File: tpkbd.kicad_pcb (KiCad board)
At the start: 2 copper layers, 43 x 38 mm, 21 parts, among them CON1 AVR-ISP-6, J1 CONN_01X02, J2 CONN_01X01, J3 USB_OTG, J4 CONN_02X20, J5 CONN_01X04, J6 GS2, J7 0, U1 ATMEGA8515-16AU, U2 AP111733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

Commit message: cleanup
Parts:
- removed CON1: AVR-ISP-6, Pin_Headers:Pin_Header_Straight_2x03
- added D1: LED, KX14:PLCC4, F.Cu at (64.6, 29.2)
- added J8: CONN_01X06, Pin_Headers:Pin_Header_Straight_1x06, F.Cu at (55.9, 59.7)
- added R6: R, Resistors_SMD:R_0603_HandSoldering, F.Cu at (63.6, 32.3)
- added R7: R, Resistors_SMD:R_0603_HandSoldering, F.Cu at (62.2, 53.2)
- added R8: R, Resistors_SMD:R_0603_HandSoldering, F.Cu at (66.8, 31.6)
- C1, C2: footprint Capacitors_SMD:C_0805_HandSoldering -> Capacitors_SMD:C_0603_HandSoldering
- C3: footprint Capacitors_SMD:C_0402 -> Capacitors_SMD:C_0603_HandSoldering
- J2: footprint Pin_Headers:Pin_Header_Straight_1x01 -> KX14:Pins1x1
- J4: value CONN_02X20 -> CONN_02X21
- R1, R2, R3, R4, R5: footprint Resistors_SMD:R_0805_HandSoldering -> Resistors_SMD:R_0603_HandSoldering
- moved J5 23.8 mm to (64.0, 26.6), turned to 90 degrees
- moved C4 10.8 mm to (55.2, 42.0), turned to 270 degrees
- moved R3 7.15 mm to (58.1, 42.1)
- moved R2 7.05 mm to (60.6, 42.1)
- moved U2 6.00 mm to (58.4, 36.0), turned to 270 degrees
- moved R4 4.77 mm to (60.6, 31.4), turned to 180 degrees
- moved C5 4.75 mm to (64.1, 39.7), turned to 45 degrees
- moved J3 4.04 mm to (57.6, 27.6)
- moved R1 3.62 mm to (63.6, 44.5), turned to 315 degrees
- moved J7 2.39 mm to (54.9, 31.4), turned to 270 degrees
- moved J2 1.17 mm to (56.4, 31.6)
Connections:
- J4 pad 42: (no net) -> Net-(J4-Pad42)
- J5 pad 1: +3V3 -> +5V
- U1 pad 10: /kb_id0 -> Net-(R3-Pad2)
- U1 pad 9: Net-(R3-Pad2) -> /led
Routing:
- net /led: track 0.00 -> 39.8 mm
- net +5V: track 79.9 -> 113.5 mm
- net /tp_rst_b: track 56.6 -> 88.4 mm, vias 2 -> 3
- net Net-(R3-Pad2): track 51.2 -> 20.2 mm
- net Net-(R2-Pad2): track 42.6 -> 15.0 mm
- net Net-(J5-Pad2): track 10.0 -> 34.9 mm
- net Net-(J3-Pad3): track 6.49 -> 19.7 mm
- net /power: track 50.2 -> 57.5 mm
- net +3V3: track 110.1 -> 103.0 mm, vias 3 -> 4
- net Net-(J3-Pad2): track 8.11 -> 13.7 mm
- net /kb_id0: track 41.7 -> 47.2 mm
- net GND: track 162.3 -> 167.2 mm, vias 1 -> 0
- net Net-(J2-Pad1): track 6.95 -> 2.37 mm
- net /B5: track 30.6 -> 34.1 mm
- net /kb_id1: track 41.6 -> 44.9 mm
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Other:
- net class Default: clearance 0.235 -> 0.3
- rule trace_clearance: 0.235 -> 0.3

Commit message: cleanup2
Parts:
- removed J1: CONN_01X02, Buttons_Switches_SMD:SW_SPST_FSMSM
- J8: value CONN_01X06 -> CONN_01X05; footprint Pin_Headers:Pin_Header_Straight_1x06 -> KX14:Pins_1x5
- moved J8 10.2 mm to (62.0, 51.5), turned to 150 degrees
- moved R7 2.59 mm to (60.8, 55.4)
- moved R1 1.30 mm to (62.4, 45.0), turned to 270 degrees
- moved C5 0.51 mm to (64.2, 39.2)
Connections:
- J4 pad 42: Net-(J4-Pad42) -> GND
- U1 pad 6: (no net) -> GND
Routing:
- net GND: track 167.2 -> 189.6 mm
- net /B5: track 34.1 -> 13.6 mm, vias 1 -> 0
- net /B7: track 32.5 -> 17.2 mm, vias 1 -> 0
- net /RST: track 23.4 -> 10.0 mm, vias 1 -> 0
- net /B6: track 28.0 -> 16.0 mm, vias 1 -> 0
- net +5V: track 113.5 -> 104.1 mm
- net /tp_rst_b: track 88.4 -> 95.5 mm
- net Net-(R2-Pad2): track 15.0 -> 19.8 mm
- net /led: track 39.8 -> 44.4 mm
- net Net-(R3-Pad2): track 20.2 -> 24.7 mm
- net Net-(J5-Pad2): track 34.9 -> 38.3 mm
- net +3V3: track 103.0 -> 100.3 mm, vias 4 -> 3
- net /kb_id0: track 47.2 -> 48.7 mm

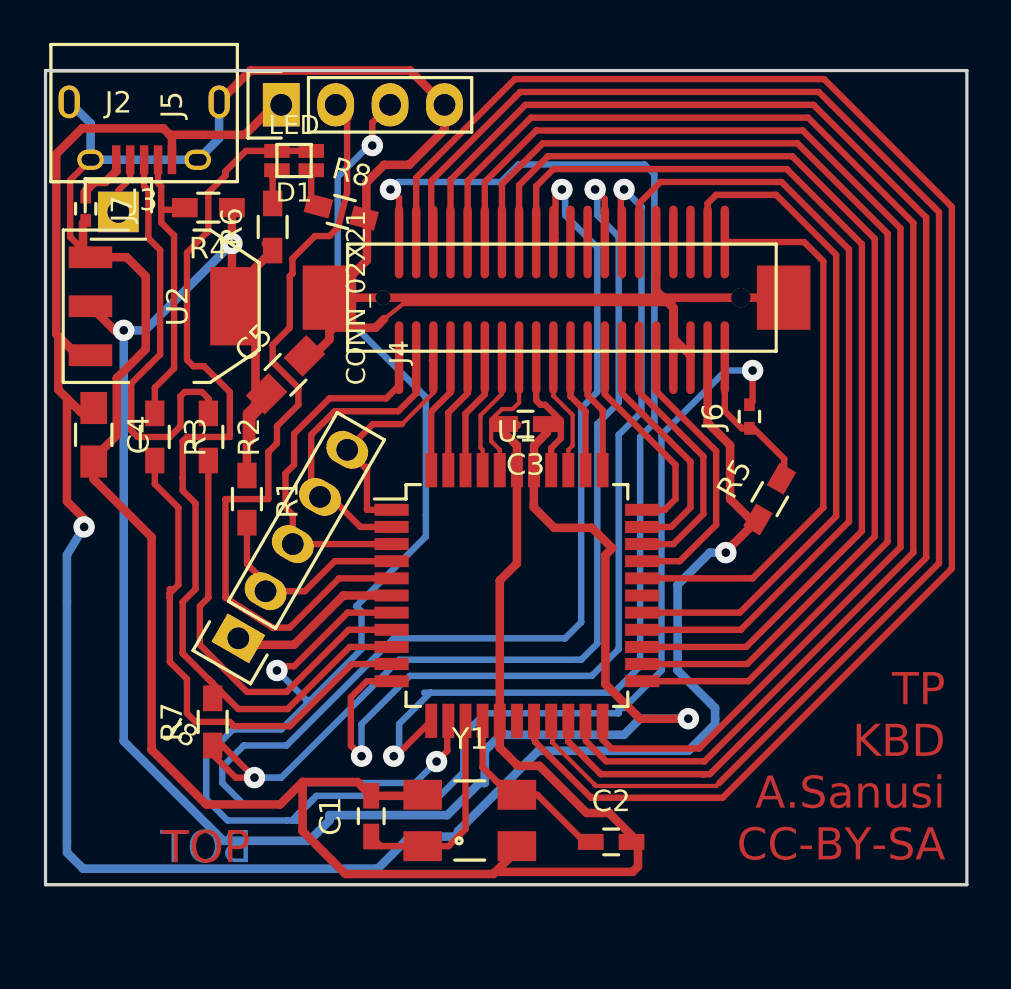
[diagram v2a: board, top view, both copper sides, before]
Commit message: add mounting holes
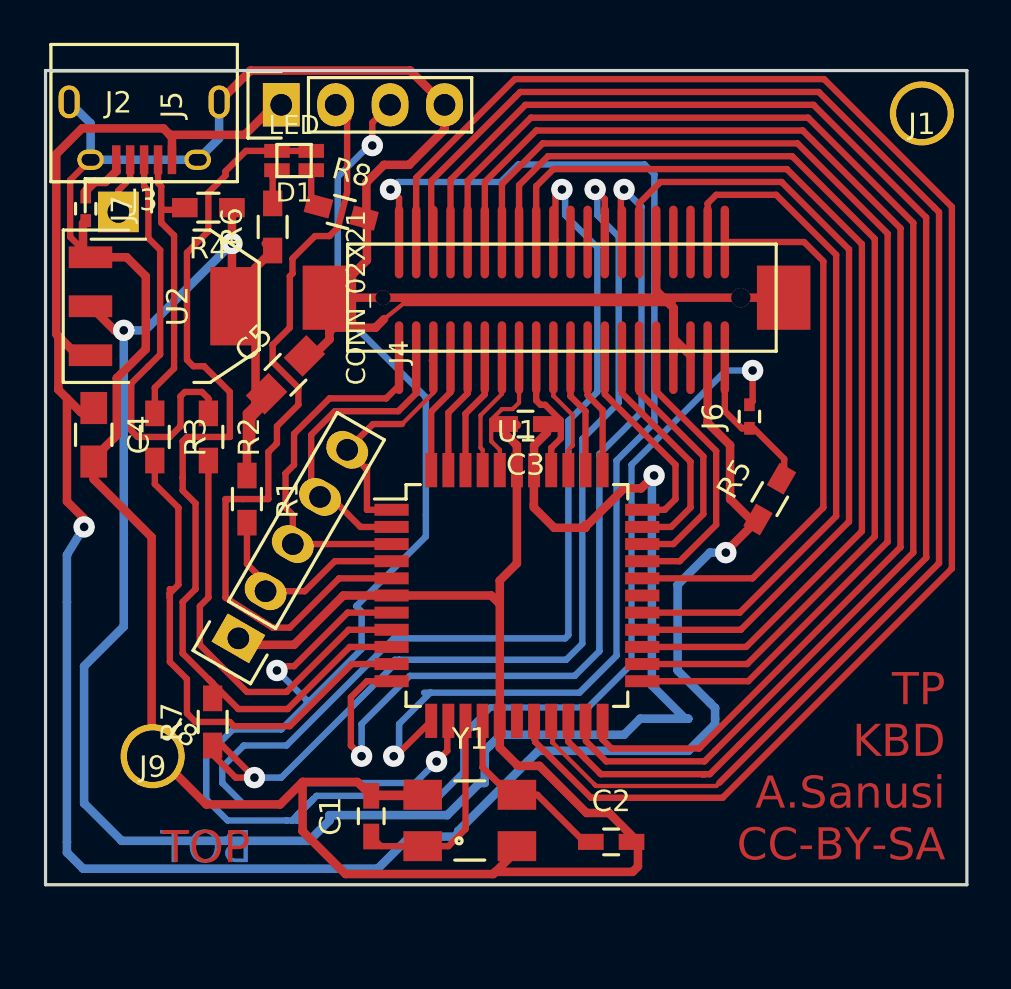
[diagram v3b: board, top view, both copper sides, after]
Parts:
- added J1: mount_2, KX14:mount_m2, F.Cu at (93.9, 27.0)
- added J9: mount_1, KX14:mount_m2, F.Cu at (58.0, 57.0)
- C1, C2: value C -> 33p
- R1: value 10k -> 1k5
- R6: value R -> 22
- R7: value R -> 1k5
- R8: value R -> 120
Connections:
- J4 pad 42: GND -> Net-(J4-Pad42)
- J4 pad 43: GND -> (no net)
- J4 pad 44: GND -> (no net)
- U1 pad 6: GND -> (no net)
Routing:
- net +3V3: track 100.3 -> 108.7 mm
- net GND: track 189.6 -> 197.3 mm
- net /hotkey: track 55.5 -> 54.6 mm
